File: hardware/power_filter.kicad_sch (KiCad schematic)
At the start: 12 parts, among them Q1 PNP, Q2 PNP

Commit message: Kicad şema düzenlemesi yapıldı.
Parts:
- removed D1: 28V, symbol Device:D_Zener
- removed D3: D, symbol Device:D
- removed Q1, Q2: PNP, symbol Simulation_SPICE:PNP
- removed R1: 6.8K, symbol Device:R
- removed R2: 1K, symbol Device:R
- removed R3: 2.2K, symbol Device:R
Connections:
- net PWR_SOURCE_VCC: now also C2.1, L1.3
- net at D2.1 (K): now also C1.1, L1.1
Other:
- note removed: "Overvoltage Protection"

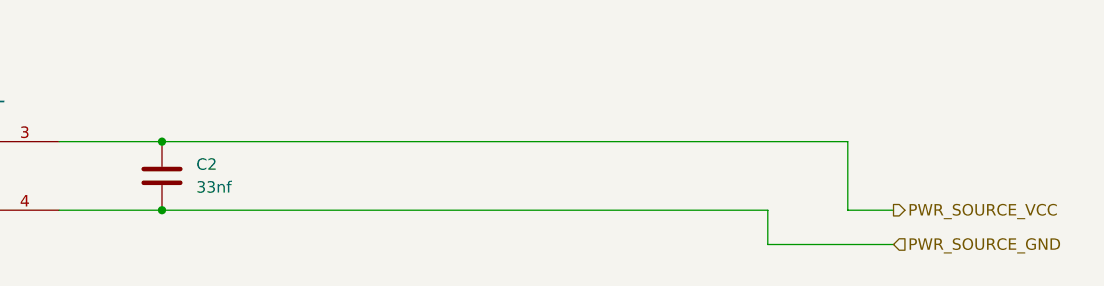
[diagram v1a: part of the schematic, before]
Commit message: Kicad Power Modülü Tamamlandı.
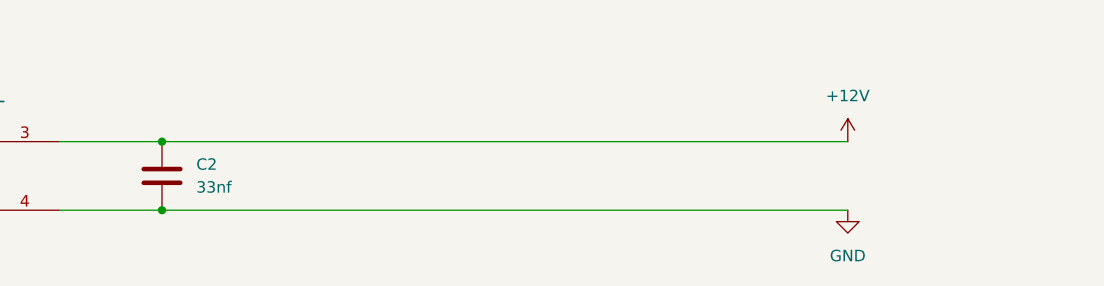
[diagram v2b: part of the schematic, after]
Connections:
- net PWR_SOURCE_GND renamed GND
- net PWR_SOURCE_VCC renamed +12V
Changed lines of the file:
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@@
-    (stroke (width 0) (type default))
-  )
-  (wire (pts (xy 234.95 48.26) (xy 248.92 48.26))
     (stroke (width 0) (type default))
   )
@@
     (stroke (width 0) (type default))
   )
-  (wire (pts (xy 234.95 44.45) (xy 234.95 48.26))
-    (stroke (width 0) (type default))
-  )
-  (wire (pts (xy 167.64 44.45) (xy 234.95 44.45))
+  (wire (pts (xy 167.64 44.45) (xy 243.84 44.45))
     (stroke (width 0) (type default))
   )
@@
     (stroke (width 0) (type default))
   )
-  (wire (pts (xy 243.84 44.45) (xy 248.92 44.45))
-    (stroke (width 0) (type default))
-  )
   (wire (pts (xy 114.3 31.75) (xy 114.3 40.64))
     (stroke (width 0) (type default))
@@
     (stroke (width 0) (type default))
   )
-  (wire (pts (xy 243.84 36.83) (xy 243.84 44.45))
-    (stroke (width 0) (type default))
-  )
   (text "Filter" (at 142.24 25.4 0)
     (effects (font (size 1.27 1.27)) (justify left bottom))
-  )
-  (hierarchical_label "PWR_SOURCE_VCC" (shape output) (at 248.92 44.45 0) (fields_autoplaced)
-    (effects (font (size 1.27 1.27)) (justify left))
-  )
-  (hierarchical_label "PWR_SOURCE_GND" (shape input) (at 248.92 48.26 0) (fields_autoplaced)
-    (effects (font (size 1.27 1.27)) (justify left))
   )
   (hierarchical_label "PWR_VCC" (shape input) (at 35.56 40.64 180) (fields_autoplaced)
@@
         )
       )
+    )
+  )
+  (symbol (lib_id "power:GND") (at 243.84 44.45 0) (unit 1)
+    (in_bom yes) (on_board yes) (dnp no) (fields_autoplaced)
+    (property "Reference" "#PWR05" (at 243.84 50.8 0)
+      (effects (font (size 1.27 1.27)) hide)
+    )
+    (property "Value" "GND" (at 243.84 49.53 0)
+      (effects (font (size 1.27 1.27)))
+    )
+    (property "Footprint" "" (at 243.84 44.45 0)
+      (effects (font (size 1.27 1.27)) hide)
+    )
+    (property "Datasheet" "" (at 243.84 44.45 0)
+      (effects (font (size 1.27 1.27)) hide)
+    )
+    (pin "1")
+    (instances
+      (project "drip-irrigation-sys-cc"
+        (path "/41708c1e-19b2-4374-83f2-108076d82b45/4f778b49-8d1a-4c8f-a914-ecde21a56ebf/06935af8-5baf-4953-9bef-44fff6202742"
+          (reference "#PWR05") (unit 1)
+        )
+      )
+    )
+  )
+  (symbol (lib_id "power:+12V") (at 243.84 36.83 0) (unit 1)
+    (in_bom yes) (on_board yes) (dnp no) (fields_autoplaced)
+    (property "Reference" "#PWR04" (at 243.84 40.64 0)
+      (effects (font (size 1.27 1.27)) hide)
+    )
+    (property "Value" "+12V" (at 243.84 31.75 0)
+      (effects (font (size 1.27 1.27)))
+    )
+    (property "Footprint" "" (at 243.84 36.83 0)
+      (effects (font (size 1.27 1.27)) hide)
+    )
+    (property "Datasheet" "" (at 243.84 36.83 0)
+      (effects (font (size 1.27 1.27)) hide)
+    )
+    (pin "1")
+    (instances
+      (project "drip-irrigation-sys-cc"
+        (path "/41708c1e-19b2-4374-83f2-108076d82b45/4f778b49-8d1a-4c8f-a914-ecde21a56ebf/06935af8-5baf-4953-9bef-44fff6202742"
+          (reference "#PWR04") (unit 1)
+        )
+      )

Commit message: Kicad şema düzenlemesi yapıldı.
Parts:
- D2: footprint (none) -> drip-irrigation-sys-cc:DIODE_DO214AA_MBRS_VIS
- L1: Digikey (none) -> 553-2181-ND
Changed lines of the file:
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@@
       (effects (font (size 1.27 1.27) italic) hide)
+    )
+    (property "Digikey" "553-2181-ND" (at 133.35 36.83 0)
+      (effects (font (size 1.27 1.27)) hide)
     )
     (pin "1")
@@
       (effects (font (size 1.27 1.27)))
     )
-    (property "Footprint" "" (at 52.07 40.64 0)
+    (property "Footprint" "drip-irrigation-sys-cc:DIODE_DO214AA_MBRS_VIS" (at 52.07 40.64 0)
       (effects (font (size 1.27 1.27)) hide)
     )

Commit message: Kicad şema düzenlemesi yapıldı.
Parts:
- renumbered C1 to C22, C2 to C23, D2 to D4
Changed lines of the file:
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@@
   (symbol (lib_id "Device:C") (at 167.64 40.64 0) (unit 1)
     (in_bom yes) (on_board yes) (dnp no)
-    (property "Reference" "C2" (at 171.45 39.37 0)
+    (property "Reference" "C23" (at 171.45 39.37 0)
       (effects (font (size 1.27 1.27)) (justify left))
     )
@@
       (project "drip-irrigation-sys-cc"
         (path "/41708c1e-19b2-4374-83f2-108076d82b45/4f778b49-8d1a-4c8f-a914-ecde21a56ebf/06935af8-5baf-4953-9bef-44fff6202742"
-          (reference "C2") (unit 1)
+          (reference "C23") (unit 1)
         )
       )
@@
   (symbol (lib_id "power:GND") (at 243.84 44.45 0) (unit 1)
     (in_bom yes) (on_board yes) (dnp no) (fields_autoplaced)
-    (property "Reference" "#PWR05" (at 243.84 50.8 0)
+    (property "Reference" "#PWR043" (at 243.84 50.8 0)
       (effects (font (size 1.27 1.27)) hide)
     )
@@
       (project "drip-irrigation-sys-cc"
         (path "/41708c1e-19b2-4374-83f2-108076d82b45/4f778b49-8d1a-4c8f-a914-ecde21a56ebf/06935af8-5baf-4953-9bef-44fff6202742"
-          (reference "#PWR05") (unit 1)
+          (reference "#PWR043") (unit 1)
         )
       )
@@
   (symbol (lib_id "power:+12V") (at 243.84 36.83 0) (unit 1)
     (in_bom yes) (on_board yes) (dnp no) (fields_autoplaced)
-    (property "Reference" "#PWR04" (at 243.84 40.64 0)
+    (property "Reference" "#PWR042" (at 243.84 40.64 0)
       (effects (font (size 1.27 1.27)) hide)
     )
@@
       (project "drip-irrigation-sys-cc"
         (path "/41708c1e-19b2-4374-83f2-108076d82b45/4f778b49-8d1a-4c8f-a914-ecde21a56ebf/06935af8-5baf-4953-9bef-44fff6202742"
-          (reference "#PWR04") (unit 1)
+          (reference "#PWR042") (unit 1)
         )
       )
@@
   (symbol (lib_id "Device:D") (at 52.07 40.64 180) (unit 1)
     (in_bom yes) (on_board yes) (dnp no) (fields_autoplaced)
-    (property "Reference" "D2" (at 52.07 34.29 0)
+    (property "Reference" "D4" (at 52.07 34.29 0)
       (effects (font (size 1.27 1.27)))
     )
@@
       (project "drip-irrigation-sys-cc"
         (path "/41708c1e-19b2-4374-83f2-108076d82b45/4f778b49-8d1a-4c8f-a914-ecde21a56ebf/06935af8-5baf-4953-9bef-44fff6202742"
-          (reference "D2") (unit 1)
+          (reference "D4") (unit 1)
         )
       )
@@
   (symbol (lib_id "Device:C") (at 124.46 40.64 0) (unit 1)
     (in_bom yes) (on_board yes) (dnp no)
-    (property "Reference" "C1" (at 128.27 39.37 0)
+    (property "Reference" "C22" (at 128.27 39.37 0)
       (effects (font (size 1.27 1.27)) (justify left))
     )
@@
       (project "drip-irrigation-sys-cc"
         (path "/41708c1e-19b2-4374-83f2-108076d82b45/4f778b49-8d1a-4c8f-a914-ecde21a56ebf/06935af8-5baf-4953-9bef-44fff6202742"
-          (reference "C1") (unit 1)
+          (reference "C22") (unit 1)
         )
       )

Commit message: PCB düzenlemesi.
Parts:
- C22, C23: footprint Capacitor_Tantalum_SMD:CP_EIA-1608-08_AVX-J -> Capacitor_SMD:C_0805_2012Metric
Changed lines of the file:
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@@
       (effects (font (size 1.27 1.27)) (justify left))
     )
-    (property "Footprint" "Capacitor_Tantalum_SMD:CP_EIA-1608-08_AVX-J" (at 168.6052 44.45 0)
+    (property "Footprint" "Capacitor_SMD:C_0805_2012Metric" (at 168.6052 44.45 0)
       (effects (font (size 1.27 1.27)) hide)
     )
@@
       (effects (font (size 1.27 1.27)) (justify left))
     )
-    (property "Footprint" "Capacitor_Tantalum_SMD:CP_EIA-1608-08_AVX-J" (at 125.4252 44.45 0)
+    (property "Footprint" "Capacitor_SMD:C_0805_2012Metric" (at 125.4252 44.45 0)
       (effects (font (size 1.27 1.27)) hide)
     )

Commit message: PCB düzenleme.
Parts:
- C22, C23: Digikey (none) -> 3372-0805B333K250BDTR-ND
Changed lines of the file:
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@@
+      (effects (font (size 1.27 1.27)) hide)
+    )
+    (property "Digikey" "3372-0805B333K250BDTR-ND" (at 167.64 40.64 0)
       (effects (font (size 1.27 1.27)) hide)
     )
@@
       (effects (font (size 1.27 1.27)) hide)
     )
+    (property "Digikey" "3372-0805B333K250BDTR-ND" (at 124.46 40.64 0)
+      (effects (font (size 1.27 1.27)) hide)
+    )
